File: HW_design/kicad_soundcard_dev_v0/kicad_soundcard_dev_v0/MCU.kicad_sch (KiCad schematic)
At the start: 44 parts, among them J2 1x6P 2.54mm SMD, J3 BM04B-SRSS-TB, J4 BM04B-SRSS-TB, J5 DM3AT-SF-PEJM5, J6 1x6P 2.54mm SMD, J7 BM04B-SRSS-TB, Q1 L8050QLT1G, Q2 L8050QLT1G, SW1 PTS636, SW2 PTS636, U3 ESP32-C6-MINI-1/U

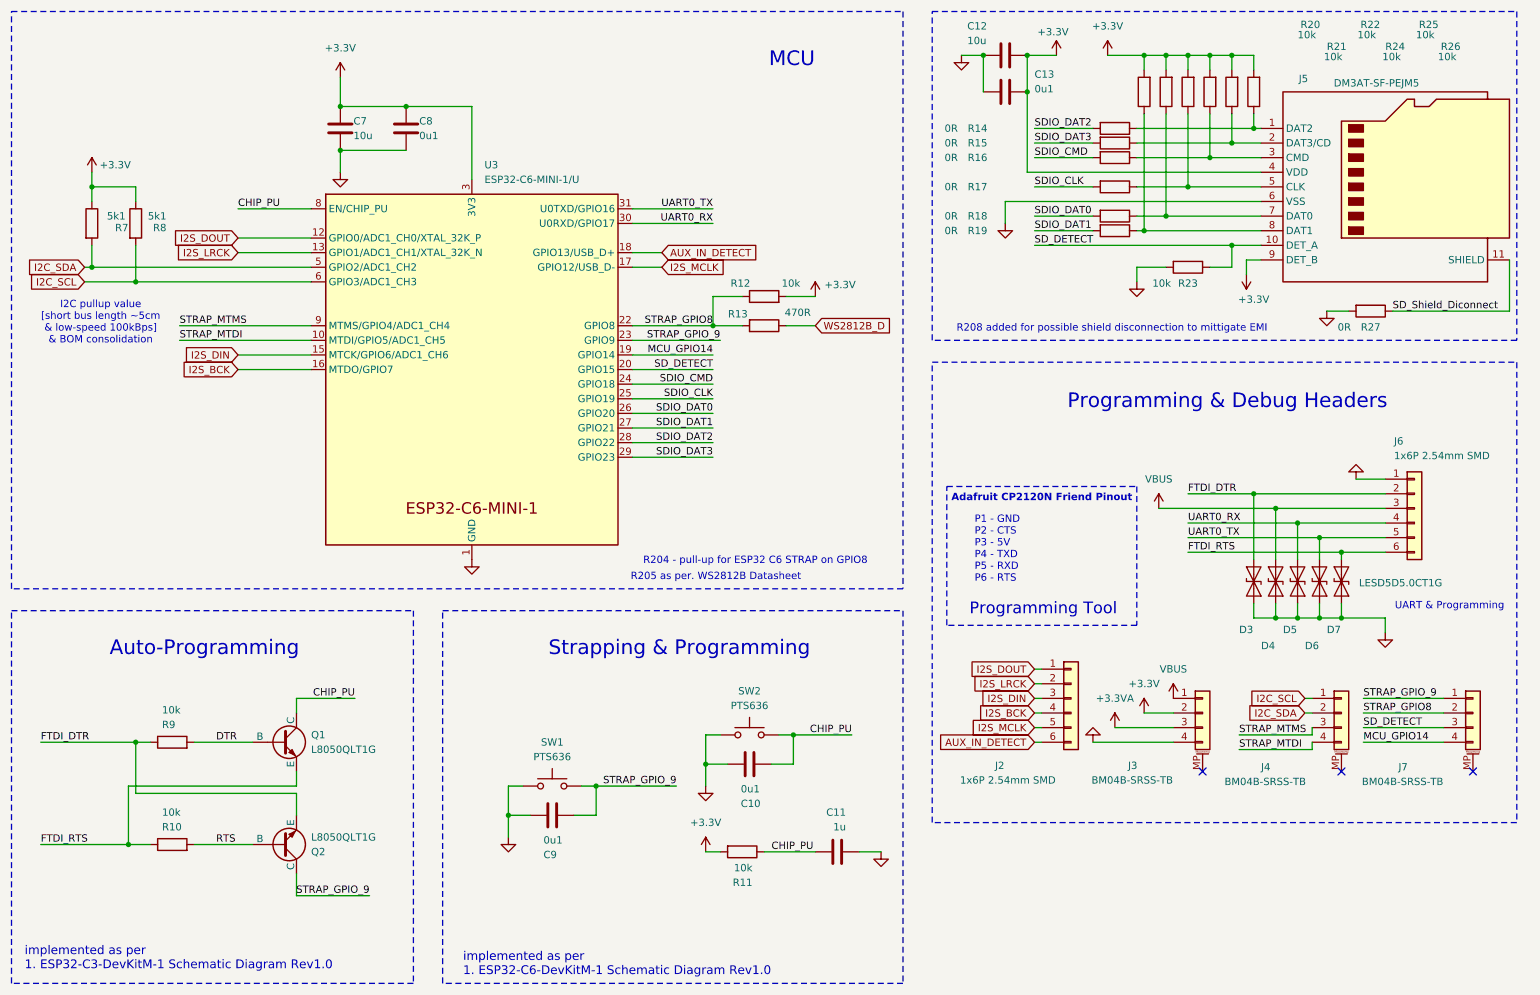
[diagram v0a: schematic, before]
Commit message: Schematic Rev2 + PCB Initial Release
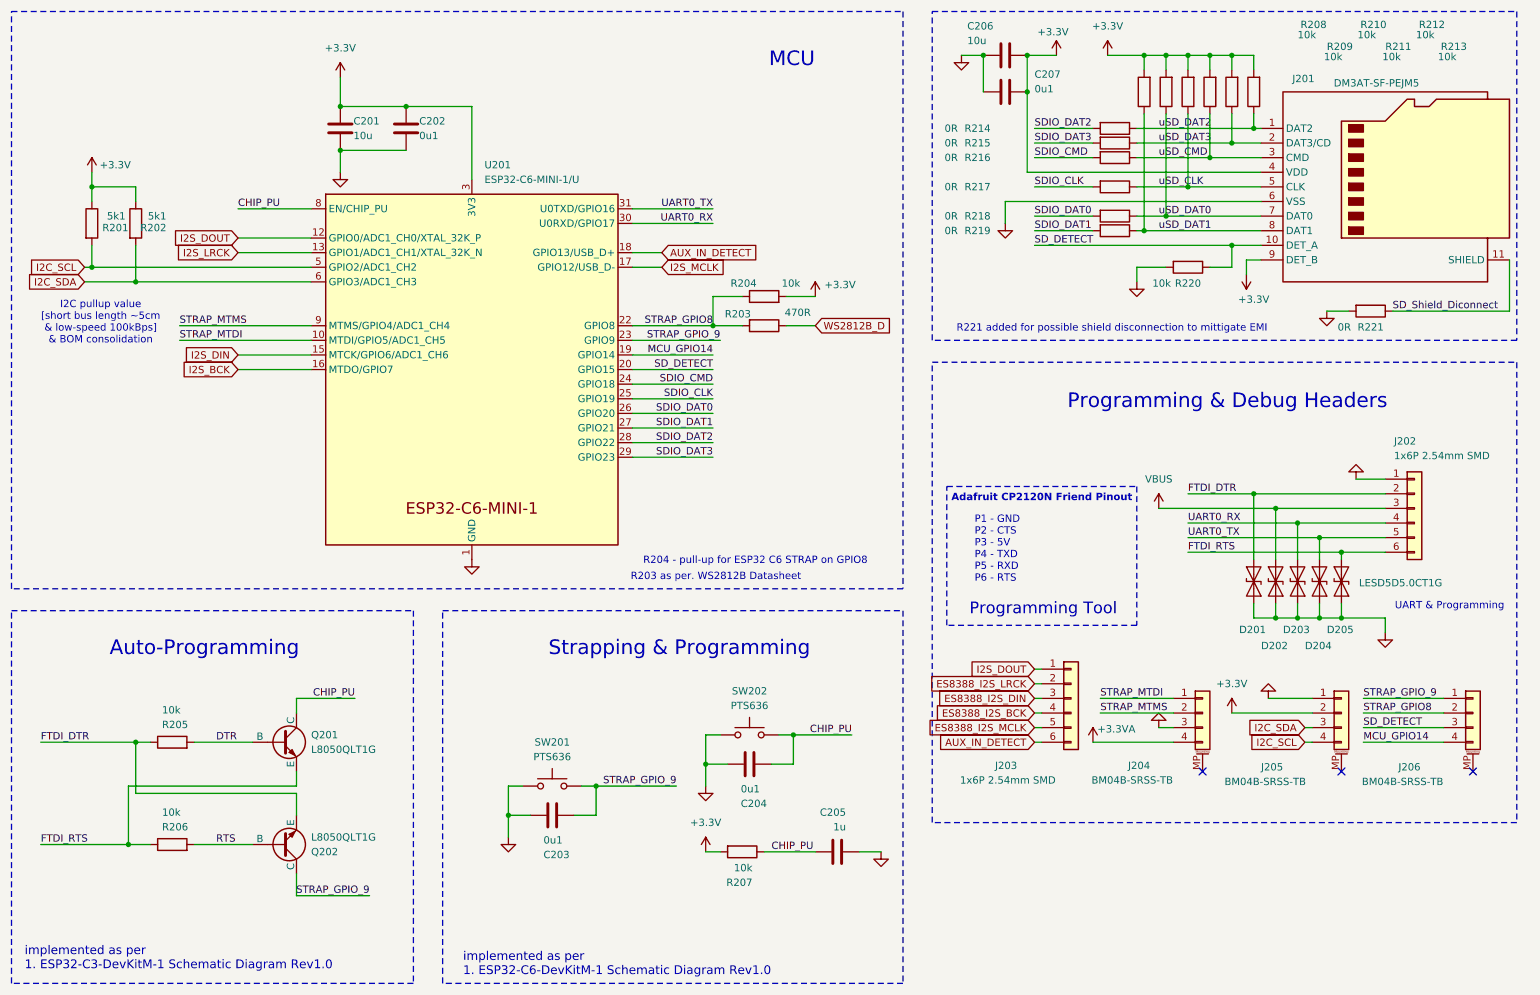
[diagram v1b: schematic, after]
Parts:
- removed SW1, SW2: PTS636, Button_Switch_SMD:SW_Tactile_SPST_NO_Straight_CK_PTS636Sx25SMTRLFS, symbol Switch:SW_MEC_5G
- added SW201, SW202: PTS636, Button_Switch_SMD:SW_Tactile_SPST_NO_Straight_CK_PTS636Sx25SMTRLFS, symbol Switch:SW_Push
- renumbered C7 to C201, C8 to C202, C9 to C203, C10 to C204, C11 to C205, C12 to C206, C13 to C207, D3 to D201, D4 to D202, D5 to D203, D6 to D204, D7 to D205, J5 to J201, J6 to J202, J2 to J203, J3 to J204, J4 to J205, J7 to J206, Q1 to Q201, Q2 to Q202, R7 to R201, R8 to R202, R13 to R203, R12 to R204, R9 to R205, R10 to R206, R11 to R207, R20 to R208, R21 to R209, R22 to R210, R24 to R211, R25 to R212, R26 to R213, R14 to R214, R15 to R215, R16 to R216, R17 to R217, R18 to R218, R19 to R219, R23 to R220, R27 to R221, U3 to U201
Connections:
- net +3.3V: now also J205.2 (Pin_2); no longer J204.2 (Pin_2)
- net +3.3VA: now also J204.4 (Pin_4); no longer J204.3 (Pin_3)
- net CHIP_PU: now also SW202.2
- net GND: now also J204.3 (Pin_3), J205.1 (Pin_1), SW201.1, SW202.1; no longer J204.4 (Pin_4)
- net I2C_SCL: now also J205.4 (Pin_4), R201.2, U201.5 (GPIO2/ADC1_CH2); no longer J205.1 (Pin_1), R202.2, U201.6 (GPIO3/ADC1_CH3)
- net I2C_SDA: now also J205.3 (Pin_3), R202.2, U201.6 (GPIO3/ADC1_CH3); no longer J205.2 (Pin_2), R201.2, U201.5 (GPIO2/ADC1_CH2)
- net I2S_BCK: no longer J203.4 (Pin_4)
- net I2S_DIN: no longer J203.3 (Pin_3)
- net I2S_LRCK: no longer J203.2 (Pin_2)
- net I2S_MCLK: no longer J203.5 (Pin_5)
- net STRAP_GPIO_9: now also SW201.2
- net STRAP_MTDI: now also J204.1 (Pin_1); no longer J205.4 (Pin_4)
- net STRAP_MTMS: now also J204.2 (Pin_2); no longer J205.3 (Pin_3)
- net VBUS: no longer J204.1 (Pin_1)
- net uSD_DAT0: now reaches J201.7 (DAT0), R209.1, R218.1
- net uSD_DAT1: now reaches J201.8 (DAT1), R208.1, R219.1
- net uSD_CLK: now reaches J201.5 (CLK), R210.1, R217.1
- net uSD_DAT2: now reaches J201.1 (DAT2), R213.1, R214.1
- net uSD_CMD: now reaches J201.3 (CMD), R211.1, R216.1
- net uSD_DAT3: now reaches J201.2 (DAT3/CD), R212.1, R215.1
- new net ES8388_I2S_BCK: J203.4 (Pin_4)
- new net ES8388_I2S_DIN: J203.3 (Pin_3)
- new net ES8388_I2S_LRCK: J203.2 (Pin_2)
- new net ES8388_I2S_MCLK: J203.5 (Pin_5)
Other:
- note added: "R203 as per. WS2812B Datasheet"
- note added: "R221 added for possible shield disconnection to mittigate EMI"
- note removed: "R205 as per. WS2812B Datasheet"
- note removed: "R208 added for possible shield disconnection to mittigate EMI"

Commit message: Production JLCPCB V0
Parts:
- C201, C206: JLCPCB Link (none) -> https://jlcpcb.com/partdetail/2043-CL10A106MQ8NNNC/C1691; Manufacturer (none) -> Samsung Electro-Mechanics; Manufacturer P/N (none) -> CL10A106MQ8NNNC
- C202, C203, C204, C207: JLCPCB Link (none) -> https://jlcpcb.com/partdetail/1877-CL05B104KO5NNNC/C1525; Manufacturer (none) -> Samsung Electro-Mechanics; Manufacturer P/N (none) -> CL05B104KO5NNNC
- C205: JLCPCB Link (none) -> https://jlcpcb.com/partdetail/15107-CL05A105KP5NNNC/C14445; Manufacturer (none) -> Samsung Electro-Mechanics; Manufacturer P/N (none) -> CL05A105KP5NNNC
- D201, D202, D203, D204, D205: JLCPCB Link (none) -> https://jlcpcb.com/partdetail/LRC-LESD5D50CT1G/C383211; Manufacturer (none) -> LRC; Manufacturer P/N (none) -> LESD5D5.0CT1G
- J201: JLCPCB Link (none) -> https://jlcpcb.com/partdetail/hrs_hirose-DM3AT_SFPEJM5/C114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; Manufacturer (none) -> HRS(Hirose); Manufacturer P/N (none) -> DM3AT-SF-PEJM5
- J202, J203: JLCPCB Link (none) -> https://jlcpcb.com/partdetail/XkbConnection-X6511WVS_06HC60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; Manufacturer (none) -> XKB Connection; Manufacturer P/N (none) -> X6511WVS-06H-C60D48R1
- J204, J205, J206: JLCPCB Link (none) -> https://jlcpcb.com/partdetail/Jst-BM04B_SRSS_TB_LF_SN/C1603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; Manufacturer (none) -> JST; Manufacturer P/N (none) -> BM04B-SRSS-TB(LF)(SN)
- Q201, Q202: JLCPCB Link (none) -> https://jlcpcb.com/partdetail/Lrc-L8050QLT1G/C49581; Manufacturer (none) -> LRC; Manufacturer P/N (none) -> L8050QLT1G
- R201, R202: JLCPCB Link (none) -> https://jlcpcb.com/partdetail/26648-0402WGF5101TCE/C25905; Manufacturer (none) -> UNI-ROYAL(Uniroyal Elec); Manufacturer P/N (none) -> 0402WGF5101TCE
- R203: JLCPCB Link (none) -> https://jlcpcb.com/partdetail/25860-0402WGF4700TCE/C25117; Manufacturer (none) -> UNI-ROYAL(Uniroyal Elec); Manufacturer P/N (none) -> 0402WGF4700TCE
- R204, R205, R206, R207, R208, R209, R210, R211, R212, R213, R220: JLCPCB Link (none) -> https://jlcpcb.com/partdetail/26487-0402WGF1002TCE/C25744; Manufacturer (none) -> UNI-ROYAL(Uniroyal Elec); Manufacturer P/N (none) -> 0402WGF1002TCE
- R214, R215, R216, R217, R218, R219, R221: JLCPCB Link (none) -> https://jlcpcb.com/partdetail/16080-0603WAJ0000T5E/C15402; Manufacturer (none) -> UNI-ROYAL(Uniroyal Elec); Manufacturer P/N (none) -> 0603WAJ0000T5E
- SW201, SW202: JLCPCB Link (none) -> https://jlcpcb.com/partdetail/ck-PTS636SK25SMTRLFS/C2689642; Manufacturer (none) -> C&K; Manufacturer P/N (none) -> PTS636SK25SMTRLFS
- U201: JLCPCB Link (none) -> https://jlcpcb.com/partdetail/ESPRESSIFINC-ESP32_C6_MINI_1N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; Manufacturer (none) -> Espressif Systems; Manufacturer P/N (none) -> ESP32-C6-MINI-1-N4
